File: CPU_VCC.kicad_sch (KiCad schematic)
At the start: 1 part

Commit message: Some DP and power work
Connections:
- net VCCSA: now reaches JCPU1.AA6 (VCCSA)
- net VCCSA: now also JCPU1.AA7 (VCCSA), JCPU1.AB6 (VCCSA), JCPU1.AB7 (VCCSA), JCPU1.AB8 (VCCSA), JCPU1.AC7 (VCCSA), JCPU1.AC8 (VCCSA), JCPU1.N7 (VCCSA), JCPU1.P7 (VCCSA), JCPU1.R7 (VCCSA), JCPU1.T7 (VCCSA), JCPU1.U7 (VCCSA), JCPU1.V7 (VCCSA), JCPU1.W7 (VCCSA), JCPU1.Y6 (VCCSA), JCPU1.Y7 (VCCSA), JCPU1.Y8 (VCCSA)
- net VCCIO: now reaches JCPU1.AJ23 (VCCIO)
- net VCCIO: now also JCPU1.AK11 (VCCIO), JCPU1.AK14 (VCCIO), JCPU1.AK24 (VCCIO), JCPU1.M8 (VCCIO), JCPU1.P8 (VCCIO), JCPU1.T8 (VCCIO), JCPU1.U8 (VCCIO), JCPU1.W8 (VCCIO)
- net VDDQ: now reaches JCPU1.AT18 (VDDQ)
- net VDDQ: now also JCPU1.AT21 (VDDQ), JCPU1.AU13 (VDDQ), JCPU1.AU15 (VDDQ), JCPU1.AU19 (VDDQ), JCPU1.AU23 (VDDQ), JCPU1.AV11 (VDDQ), JCPU1.AV17 (VDDQ), JCPU1.AV21 (VDDQ), JCPU1.AW10 (VDDQ), JCPU1.AW14 (VDDQ), JCPU1.AW25 (VDDQ), JCPU1.AY12 (VDDQ), JCPU1.AY16 (VDDQ), JCPU1.AY18 (VDDQ), JCPU1.AY23 (VDDQ)
- net VCCST: now reaches JCPU1.V5 (VCCST)
- net VCCST: now also JCPU1.V6 (VCCST)
- net VCC_CORE: now reaches JCPU1.A25 (VCC_CORE)
- net VCC_CORE: now also JCPU1.A26 (VCC_CORE), JCPU1.A27 (VCC_CORE), JCPU1.A28 (VCC_CORE), JCPU1.A29 (VCC_CORE), JCPU1.A30 (VCC_CORE), JCPU1.AJ11 (VCC_CORE), JCPU1.AJ12 (VCC_CORE), JCPU1.AJ13 (VCC_CORE), JCPU1.AJ14 (VCC_CORE), JCPU1.AJ15 (VCC_CORE), JCPU1.AJ16 (VCC_CORE), JCPU1.AJ17 (VCC_CORE), JCPU1.AJ18 (VCC_CORE), JCPU1.AJ19 (VCC_CORE), JCPU1.AJ20 (VCC_CORE), JCPU1.AJ21 (VCC_CORE), JCPU1.AJ25 (VCC_CORE), JCPU1.AJ26 (VCC_CORE), JCPU1.AJ27 (VCC_CORE), JCPU1.AJ28 (VCC_CORE), JCPU1.AJ29 (VCC_CORE), JCPU1.AK21 (VCC_CORE), JCPU1.B25 (VCC_CORE), JCPU1.B27 (VCC_CORE), JCPU1.B29 (VCC_CORE), JCPU1.B31 (VCC_CORE), JCPU1.B32 (VCC_CORE), JCPU1.B33 (VCC_CORE), JCPU1.B34 (VCC_CORE), JCPU1.B35 (VCC_CORE), JCPU1.B36 (VCC_CORE), JCPU1.B37 (VCC_CORE), JCPU1.C25 (VCC_CORE), JCPU1.C26 (VCC_CORE), JCPU1.C27 (VCC_CORE), JCPU1.C28 (VCC_CORE), JCPU1.C29 (VCC_CORE), JCPU1.C30 (VCC_CORE), JCPU1.C32 (VCC_CORE), JCPU1.C34 (VCC_CORE), JCPU1.C36 (VCC_CORE), JCPU1.D25 (VCC_CORE), JCPU1.D27 (VCC_CORE), JCPU1.D29 (VCC_CORE), JCPU1.D31 (VCC_CORE), JCPU1.D32 (VCC_CORE), JCPU1.D33 (VCC_CORE), JCPU1.D34 (VCC_CORE), JCPU1.D35 (VCC_CORE), JCPU1.D36 (VCC_CORE), JCPU1.E24 (VCC_CORE), JCPU1.E25 (VCC_CORE), JCPU1.E26 (VCC_CORE), JCPU1.E27 (VCC_CORE), JCPU1.E28 (VCC_CORE), JCPU1.E29 (VCC_CORE), JCPU1.E30 (VCC_CORE), JCPU1.E32 (VCC_CORE), JCPU1.E34 (VCC_CORE), JCPU1.E36 (VCC_CORE), JCPU1.F23 (VCC_CORE), JCPU1.F24 (VCC_CORE), JCPU1.F25 (VCC_CORE), JCPU1.F27 (VCC_CORE), JCPU1.F29 (VCC_CORE), JCPU1.F31 (VCC_CORE), JCPU1.F32 (VCC_CORE), JCPU1.F33 (VCC_CORE), JCPU1.F34 (VCC_CORE), JCPU1.F35 (VCC_CORE), JCPU1.F37 (VCC_CORE), JCPU1.G23 (VCC_CORE), JCPU1.G24 (VCC_CORE), JCPU1.G25 (VCC_CORE), JCPU1.G26 (VCC_CORE), JCPU1.G27 (VCC_CORE), JCPU1.G28 (VCC_CORE), JCPU1.G29 (VCC_CORE), JCPU1.G30 (VCC_CORE), JCPU1.G32 (VCC_CORE), JCPU1.G34 (VCC_CORE), JCPU1.G35 (VCC_CORE), JCPU1.H22 (VCC_CORE), JCPU1.H23 (VCC_CORE), JCPU1.H25 (VCC_CORE), JCPU1.H27 (VCC_CORE), JCPU1.H29 (VCC_CORE), JCPU1.H31 (VCC_CORE), JCPU1.H32 (VCC_CORE), JCPU1.H33 (VCC_CORE), JCPU1.H34 (VCC_CORE), JCPU1.J21 (VCC_CORE), JCPU1.J22 (VCC_CORE), JCPU1.J23 (VCC_CORE), JCPU1.J24 (VCC_CORE), JCPU1.J25 (VCC_CORE), JCPU1.J26 (VCC_CORE), JCPU1.J27 (VCC_CORE), JCPU1.J28 (VCC_CORE), JCPU1.J29 (VCC_CORE), JCPU1.J30 (VCC_CORE), JCPU1.J31 (VCC_CORE), JCPU1.J33 (VCC_CORE), JCPU1.J35 (VCC_CORE), JCPU1.K16 (VCC_CORE), JCPU1.K18 (VCC_CORE), JCPU1.K20 (VCC_CORE), JCPU1.K21 (VCC_CORE), JCPU1.K23 (VCC_CORE), JCPU1.K25 (VCC_CORE), JCPU1.K27 (VCC_CORE), JCPU1.K29 (VCC_CORE), JCPU1.K31 (VCC_CORE), JCPU1.K32 (VCC_CORE), JCPU1.K34 (VCC_CORE), JCPU1.L14 (VCC_CORE), JCPU1.L15 (VCC_CORE), JCPU1.L16 (VCC_CORE), JCPU1.L17 (VCC_CORE), JCPU1.L18 (VCC_CORE), JCPU1.L19 (VCC_CORE), JCPU1.L20 (VCC_CORE), JCPU1.L21 (VCC_CORE), JCPU1.L22 (VCC_CORE), JCPU1.L23 (VCC_CORE), JCPU1.L24 (VCC_CORE), JCPU1.L25 (VCC_CORE), JCPU1.L26 (VCC_CORE), JCPU1.L27 (VCC_CORE), JCPU1.L28 (VCC_CORE), JCPU1.L29 (VCC_CORE), JCPU1.L30 (VCC_CORE), JCPU1.L31 (VCC_CORE), JCPU1.L33 (VCC_CORE), JCPU1.M13 (VCC_CORE), JCPU1.M14 (VCC_CORE), JCPU1.M16 (VCC_CORE), JCPU1.M18 (VCC_CORE), JCPU1.M20 (VCC_CORE), JCPU1.M22 (VCC_CORE), JCPU1.M24 (VCC_CORE), JCPU1.M26 (VCC_CORE), JCPU1.M28 (VCC_CORE), JCPU1.M30 (VCC_CORE), JCPU1.M32 (VCC_CORE)
- net VCC_iGPU: now reaches JCPU1.AA34 (VCCGT)
- net VCC_iGPU: now also JCPU1.AA35 (VCCGT), JCPU1.AA36 (VCCGT), JCPU1.AA37 (VCCGT), JCPU1.AA38 (VCCGT), JCPU1.AB33 (VCCGT), JCPU1.AB34 (VCCGT), JCPU1.G36 (VCCGT), JCPU1.G37 (VCCGT), JCPU1.G38 (VCCGT), JCPU1.G39 (VCCGT), JCPU1.G40 (VCCGT), JCPU1.H36 (VCCGT), JCPU1.H38 (VCCGT), JCPU1.H40 (VCCGT), JCPU1.J36 (VCCGT), JCPU1.J37 (VCCGT), JCPU1.J38 (VCCGT), JCPU1.J39 (VCCGT), JCPU1.J40 (VCCGT), JCPU1.K36 (VCCGT), JCPU1.K38 (VCCGT), JCPU1.K40 (VCCGT), JCPU1.L34 (VCCGT), JCPU1.L35 (VCCGT), JCPU1.L36 (VCCGT), JCPU1.L37 (VCCGT), JCPU1.L38 (VCCGT), JCPU1.L39 (VCCGT), JCPU1.L40 (VCCGT), JCPU1.M33 (VCCGT), JCPU1.M34 (VCCGT), JCPU1.M36 (VCCGT), JCPU1.M38 (VCCGT), JCPU1.M40 (VCCGT), JCPU1.N34 (VCCGT), JCPU1.N35 (VCCGT), JCPU1.N36 (VCCGT), JCPU1.N37 (VCCGT), JCPU1.N38 (VCCGT), JCPU1.N39 (VCCGT), JCPU1.N40 (VCCGT), JCPU1.P33 (VCCGT), JCPU1.P34 (VCCGT), JCPU1.P36 (VCCGT), JCPU1.P38 (VCCGT), JCPU1.P40 (VCCGT), JCPU1.R34 (VCCGT), JCPU1.R35 (VCCGT), JCPU1.R36 (VCCGT), JCPU1.R37 (VCCGT), JCPU1.R38 (VCCGT), JCPU1.R39 (VCCGT), JCPU1.R40 (VCCGT), JCPU1.T33 (VCCGT), JCPU1.T34 (VCCGT), JCPU1.T36 (VCCGT), JCPU1.T38 (VCCGT), JCPU1.T40 (VCCGT), JCPU1.U34 (VCCGT), JCPU1.U35 (VCCGT), JCPU1.U36 (VCCGT), JCPU1.U37 (VCCGT), JCPU1.U38 (VCCGT), JCPU1.U39 (VCCGT), JCPU1.U40 (VCCGT), JCPU1.V33 (VCCGT), JCPU1.V34 (VCCGT), JCPU1.V36 (VCCGT), JCPU1.V38 (VCCGT), JCPU1.V40 (VCCGT), JCPU1.W34 (VCCGT), JCPU1.W35 (VCCGT), JCPU1.W36 (VCCGT), JCPU1.W37 (VCCGT), JCPU1.W38 (VCCGT), JCPU1.Y33 (VCCGT), JCPU1.Y34 (VCCGT), JCPU1.Y36 (VCCGT), JCPU1.Y38 (VCCGT)

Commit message: Added LGA1151 socket bracket holes
stolen from another lga1151 footprint that has wrong pin numbers....
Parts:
- JCPU1: footprint A-my-stuff:LGA-1151_L47.1-W42.5-P0.91_PE115127-4041-01H -> A-my-stuff:LGA1151_TE-2287402-1
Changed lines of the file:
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@@
 			)
 		)
-		(property "Footprint" "A-my-stuff:LGA-1151_L47.1-W42.5-P0.91_PE115127-4041-01H"
+		(property "Footprint" "A-my-stuff:LGA1151_TE-2287402-1"
 			(at 203.2 256.54 0)
 			(effects
@@
 			)
 		)
-		(property "Footprint" "A-my-stuff:LGA-1151_L47.1-W42.5-P0.91_PE115127-4041-01H"
+		(property "Footprint" "A-my-stuff:LGA1151_TE-2287402-1"
 			(at 76.2 256.54 0)
 			(effects
@@
 			)
 		)
-		(property "Footprint" "A-my-stuff:LGA-1151_L47.1-W42.5-P0.91_PE115127-4041-01H"
+		(property "Footprint" "A-my-stuff:LGA1151_TE-2287402-1"
 			(at 139.7 256.54 0)
 			(effects

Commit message: Added CPU CFG resistors
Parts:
- JCPU1: footprint A-my-stuff:LGA1151_TE-2287402-1 -> A-my-stuff:LGA-1151_L47.1-W42.5-P0.91_PE115127-4041-01H
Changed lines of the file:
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@@
 			)
 		)
-		(property "Footprint" "A-my-stuff:LGA1151_TE-2287402-1"
+		(property "Footprint" "A-my-stuff:LGA-1151_L47.1-W42.5-P0.91_PE115127-4041-01H"
 			(at 203.2 256.54 0)
 			(effects
@@
 			)
 		)
-		(property "Footprint" "A-my-stuff:LGA1151_TE-2287402-1"
+		(property "Footprint" "A-my-stuff:LGA-1151_L47.1-W42.5-P0.91_PE115127-4041-01H"
 			(at 76.2 256.54 0)
 			(effects
@@
 			)
 		)
-		(property "Footprint" "A-my-stuff:LGA1151_TE-2287402-1"
+		(property "Footprint" "A-my-stuff:LGA-1151_L47.1-W42.5-P0.91_PE115127-4041-01H"
 			(at 139.7 256.54 0)
 			(effects

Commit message: stroopwafel.exe
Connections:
- net VCCIO: no longer JCPU1.AJ23 (VCCIO), JCPU1.AK11 (VCCIO), JCPU1.AK14 (VCCIO), JCPU1.AK24 (VCCIO), JCPU1.M8 (VCCIO), JCPU1.P8 (VCCIO), JCPU1.T8 (VCCIO), JCPU1.U8 (VCCIO), JCPU1.W8 (VCCIO)
- net VCCSA: no longer JCPU1.AA6 (VCCSA), JCPU1.AA7 (VCCSA), JCPU1.AB6 (VCCSA), JCPU1.AB7 (VCCSA), JCPU1.AB8 (VCCSA), JCPU1.AC7 (VCCSA), JCPU1.AC8 (VCCSA), JCPU1.N7 (VCCSA), JCPU1.P7 (VCCSA), JCPU1.R7 (VCCSA), JCPU1.T7 (VCCSA), JCPU1.U7 (VCCSA), JCPU1.V7 (VCCSA), JCPU1.W7 (VCCSA), JCPU1.Y6 (VCCSA), JCPU1.Y7 (VCCSA), JCPU1.Y8 (VCCSA)
- net VCCST: no longer JCPU1.V5 (VCCST), JCPU1.V6 (VCCST)
- net VCC_CORE: no longer JCPU1.A25 (VCC_CORE), JCPU1.A26 (VCC_CORE), JCPU1.A27 (VCC_CORE), JCPU1.A28 (VCC_CORE), JCPU1.A29 (VCC_CORE), JCPU1.A30 (VCC_CORE), JCPU1.AJ11 (VCC_CORE), JCPU1.AJ12 (VCC_CORE), JCPU1.AJ13 (VCC_CORE), JCPU1.AJ14 (VCC_CORE), JCPU1.AJ15 (VCC_CORE), JCPU1.AJ16 (VCC_CORE), JCPU1.AJ17 (VCC_CORE), JCPU1.AJ18 (VCC_CORE), JCPU1.AJ19 (VCC_CORE), JCPU1.AJ20 (VCC_CORE), JCPU1.AJ21 (VCC_CORE), JCPU1.AJ25 (VCC_CORE), JCPU1.AJ26 (VCC_CORE), JCPU1.AJ27 (VCC_CORE), JCPU1.AJ28 (VCC_CORE), JCPU1.AJ29 (VCC_CORE), JCPU1.AK21 (VCC_CORE), JCPU1.B25 (VCC_CORE), JCPU1.B27 (VCC_CORE), JCPU1.B29 (VCC_CORE), JCPU1.B31 (VCC_CORE), JCPU1.B32 (VCC_CORE), JCPU1.B33 (VCC_CORE), JCPU1.B34 (VCC_CORE), JCPU1.B35 (VCC_CORE), JCPU1.B36 (VCC_CORE), JCPU1.B37 (VCC_CORE), JCPU1.C25 (VCC_CORE), JCPU1.C26 (VCC_CORE), JCPU1.C27 (VCC_CORE), JCPU1.C28 (VCC_CORE), JCPU1.C29 (VCC_CORE), JCPU1.C30 (VCC_CORE), JCPU1.C32 (VCC_CORE), JCPU1.C34 (VCC_CORE), JCPU1.C36 (VCC_CORE), JCPU1.D25 (VCC_CORE), JCPU1.D27 (VCC_CORE), JCPU1.D29 (VCC_CORE), JCPU1.D31 (VCC_CORE), JCPU1.D32 (VCC_CORE), JCPU1.D33 (VCC_CORE), JCPU1.D34 (VCC_CORE), JCPU1.D35 (VCC_CORE), JCPU1.D36 (VCC_CORE), JCPU1.E24 (VCC_CORE), JCPU1.E25 (VCC_CORE), JCPU1.E26 (VCC_CORE), JCPU1.E27 (VCC_CORE), JCPU1.E28 (VCC_CORE), JCPU1.E29 (VCC_CORE), JCPU1.E30 (VCC_CORE), JCPU1.E32 (VCC_CORE), JCPU1.E34 (VCC_CORE), JCPU1.E36 (VCC_CORE), JCPU1.F23 (VCC_CORE), JCPU1.F24 (VCC_CORE), JCPU1.F25 (VCC_CORE), JCPU1.F27 (VCC_CORE), JCPU1.F29 (VCC_CORE), JCPU1.F31 (VCC_CORE), JCPU1.F32 (VCC_CORE), JCPU1.F33 (VCC_CORE), JCPU1.F34 (VCC_CORE), JCPU1.F35 (VCC_CORE), JCPU1.F37 (VCC_CORE), JCPU1.G23 (VCC_CORE), JCPU1.G24 (VCC_CORE), JCPU1.G25 (VCC_CORE), JCPU1.G26 (VCC_CORE), JCPU1.G27 (VCC_CORE), JCPU1.G28 (VCC_CORE), JCPU1.G29 (VCC_CORE), JCPU1.G30 (VCC_CORE), JCPU1.G32 (VCC_CORE), JCPU1.G34 (VCC_CORE), JCPU1.G35 (VCC_CORE), JCPU1.H22 (VCC_CORE), JCPU1.H23 (VCC_CORE), JCPU1.H25 (VCC_CORE), JCPU1.H27 (VCC_CORE), JCPU1.H29 (VCC_CORE), JCPU1.H31 (VCC_CORE), JCPU1.H32 (VCC_CORE), JCPU1.H33 (VCC_CORE), JCPU1.H34 (VCC_CORE), JCPU1.J21 (VCC_CORE), JCPU1.J22 (VCC_CORE), JCPU1.J23 (VCC_CORE), JCPU1.J24 (VCC_CORE), JCPU1.J25 (VCC_CORE), JCPU1.J26 (VCC_CORE), JCPU1.J27 (VCC_CORE), JCPU1.J28 (VCC_CORE), JCPU1.J29 (VCC_CORE), JCPU1.J30 (VCC_CORE), JCPU1.J31 (VCC_CORE), JCPU1.J33 (VCC_CORE), JCPU1.J35 (VCC_CORE), JCPU1.K16 (VCC_CORE), JCPU1.K18 (VCC_CORE), JCPU1.K20 (VCC_CORE), JCPU1.K21 (VCC_CORE), JCPU1.K23 (VCC_CORE), JCPU1.K25 (VCC_CORE), JCPU1.K27 (VCC_CORE), JCPU1.K29 (VCC_CORE), JCPU1.K31 (VCC_CORE), JCPU1.K32 (VCC_CORE), JCPU1.K34 (VCC_CORE), JCPU1.L14 (VCC_CORE), JCPU1.L15 (VCC_CORE), JCPU1.L16 (VCC_CORE), JCPU1.L17 (VCC_CORE), JCPU1.L18 (VCC_CORE), JCPU1.L19 (VCC_CORE), JCPU1.L20 (VCC_CORE), JCPU1.L21 (VCC_CORE), JCPU1.L22 (VCC_CORE), JCPU1.L23 (VCC_CORE), JCPU1.L24 (VCC_CORE), JCPU1.L25 (VCC_CORE), JCPU1.L26 (VCC_CORE), JCPU1.L27 (VCC_CORE), JCPU1.L28 (VCC_CORE), JCPU1.L29 (VCC_CORE), JCPU1.L30 (VCC_CORE), JCPU1.L31 (VCC_CORE), JCPU1.L33 (VCC_CORE), JCPU1.M13 (VCC_CORE), JCPU1.M14 (VCC_CORE), JCPU1.M16 (VCC_CORE), JCPU1.M18 (VCC_CORE), JCPU1.M20 (VCC_CORE), JCPU1.M22 (VCC_CORE), JCPU1.M24 (VCC_CORE), JCPU1.M26 (VCC_CORE), JCPU1.M28 (VCC_CORE), JCPU1.M30 (VCC_CORE), JCPU1.M32 (VCC_CORE)
- net VCC_iGPU: no longer JCPU1.AA34 (VCCGT), JCPU1.AA35 (VCCGT), JCPU1.AA36 (VCCGT), JCPU1.AA37 (VCCGT), JCPU1.AA38 (VCCGT), JCPU1.AB33 (VCCGT), JCPU1.AB34 (VCCGT), JCPU1.G36 (VCCGT), JCPU1.G37 (VCCGT), JCPU1.G38 (VCCGT), JCPU1.G39 (VCCGT), JCPU1.G40 (VCCGT), JCPU1.H36 (VCCGT), JCPU1.H38 (VCCGT), JCPU1.H40 (VCCGT), JCPU1.J36 (VCCGT), JCPU1.J37 (VCCGT), JCPU1.J38 (VCCGT), JCPU1.J39 (VCCGT), JCPU1.J40 (VCCGT), JCPU1.K36 (VCCGT), JCPU1.K38 (VCCGT), JCPU1.K40 (VCCGT), JCPU1.L34 (VCCGT), JCPU1.L35 (VCCGT), JCPU1.L36 (VCCGT), JCPU1.L37 (VCCGT), JCPU1.L38 (VCCGT), JCPU1.L39 (VCCGT), JCPU1.L40 (VCCGT), JCPU1.M33 (VCCGT), JCPU1.M34 (VCCGT), JCPU1.M36 (VCCGT), JCPU1.M38 (VCCGT), JCPU1.M40 (VCCGT), JCPU1.N34 (VCCGT), JCPU1.N35 (VCCGT), JCPU1.N36 (VCCGT), JCPU1.N37 (VCCGT), JCPU1.N38 (VCCGT), JCPU1.N39 (VCCGT), JCPU1.N40 (VCCGT), JCPU1.P33 (VCCGT), JCPU1.P34 (VCCGT), JCPU1.P36 (VCCGT), JCPU1.P38 (VCCGT), JCPU1.P40 (VCCGT), JCPU1.R34 (VCCGT), JCPU1.R35 (VCCGT), JCPU1.R36 (VCCGT), JCPU1.R37 (VCCGT), JCPU1.R38 (VCCGT), JCPU1.R39 (VCCGT), JCPU1.R40 (VCCGT), JCPU1.T33 (VCCGT), JCPU1.T34 (VCCGT), JCPU1.T36 (VCCGT), JCPU1.T38 (VCCGT), JCPU1.T40 (VCCGT), JCPU1.U34 (VCCGT), JCPU1.U35 (VCCGT), JCPU1.U36 (VCCGT), JCPU1.U37 (VCCGT), JCPU1.U38 (VCCGT), JCPU1.U39 (VCCGT), JCPU1.U40 (VCCGT), JCPU1.V33 (VCCGT), JCPU1.V34 (VCCGT), JCPU1.V36 (VCCGT), JCPU1.V38 (VCCGT), JCPU1.V40 (VCCGT), JCPU1.W34 (VCCGT), JCPU1.W35 (VCCGT), JCPU1.W36 (VCCGT), JCPU1.W37 (VCCGT), JCPU1.W38 (VCCGT), JCPU1.Y33 (VCCGT), JCPU1.Y34 (VCCGT), JCPU1.Y36 (VCCGT), JCPU1.Y38 (VCCGT)
- net VDDQ: no longer JCPU1.AT18 (VDDQ), JCPU1.AT21 (VDDQ), JCPU1.AU13 (VDDQ), JCPU1.AU15 (VDDQ), JCPU1.AU19 (VDDQ), JCPU1.AU23 (VDDQ), JCPU1.AV11 (VDDQ), JCPU1.AV17 (VDDQ), JCPU1.AV21 (VDDQ), JCPU1.AW10 (VDDQ), JCPU1.AW14 (VDDQ), JCPU1.AW25 (VDDQ), JCPU1.AY12 (VDDQ), JCPU1.AY16 (VDDQ), JCPU1.AY18 (VDDQ), JCPU1.AY23 (VDDQ)
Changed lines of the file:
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@@
 		(lib_id "A-my-stuff:Intel_CFL_1151")
 		(at 203.2 144.78 0)
-		(unit 9)
+		(unit 1)
 		(exclude_from_sim no)
 		(in_bom yes)
@@
 		(pin "J5"
 		)
-		(instances
-			(project ""
-				(path "/4bc771b8-eb19-46d0-8798-27231a7c6e83/061fe2d6-87c2-48c2-90bb-0928700512fc"
-					(reference "JCPU1")
-					(unit 9)
-				)
-				(path "/4bc771b8-eb19-46d0-8798-27231a7c6e83/5036d382-d60b-4069-a42a-4bbea2c68172"
-					(reference "JCPU1")
-					(unit 9)
-				)
-			)
-		)
 	)
 	(symbol
@@
 		(lib_id "A-my-stuff:Intel_CFL_1151")
 		(at 76.2 144.78 0)
-		(unit 7)
+		(unit 1)
 		(exclude_from_sim no)
 		(in_bom yes)
@@
 		(pin "J5"
 		)
-		(instances
-			(project ""
-				(path "/4bc771b8-eb19-46d0-8798-27231a7c6e83/061fe2d6-87c2-48c2-90bb-0928700512fc"
-					(reference "JCPU1")
-					(unit 7)
-				)
-				(path "/4bc771b8-eb19-46d0-8798-27231a7c6e83/5036d382-d60b-4069-a42a-4bbea2c68172"
-					(reference "JCPU1")
-					(unit 7)
-				)
-			)
-		)
 	)
 	(symbol
@@
 		(lib_id "A-my-stuff:Intel_CFL_1151")
 		(at 139.7 144.78 0)
-		(unit 8)
+		(unit 1)
 		(exclude_from_sim no)
 		(in_bom yes)
@@
 		(pin "J5"
 		)
-		(instances
-			(project ""
-				(path "/4bc771b8-eb19-46d0-8798-27231a7c6e83/061fe2d6-87c2-48c2-90bb-0928700512fc"
-					(reference "JCPU1")
-					(unit 8)
-				)
-				(path "/4bc771b8-eb19-46d0-8798-27231a7c6e83/5036d382-d60b-4069-a42a-4bbea2c68172"
-					(reference "JCPU1")
-					(unit 8)
-				)
-			)
-		)
 	)
 	(symbol
@@
 		(pin "1"
 		)
-		(instances
-			(project ""
-				(path "/4bc771b8-eb19-46d0-8798-27231a7c6e83/5036d382-d60b-4069-a42a-4bbea2c68172"
-					(reference "#PWR011")
-					(unit 1)
-				)
-			)
-		)
 	)

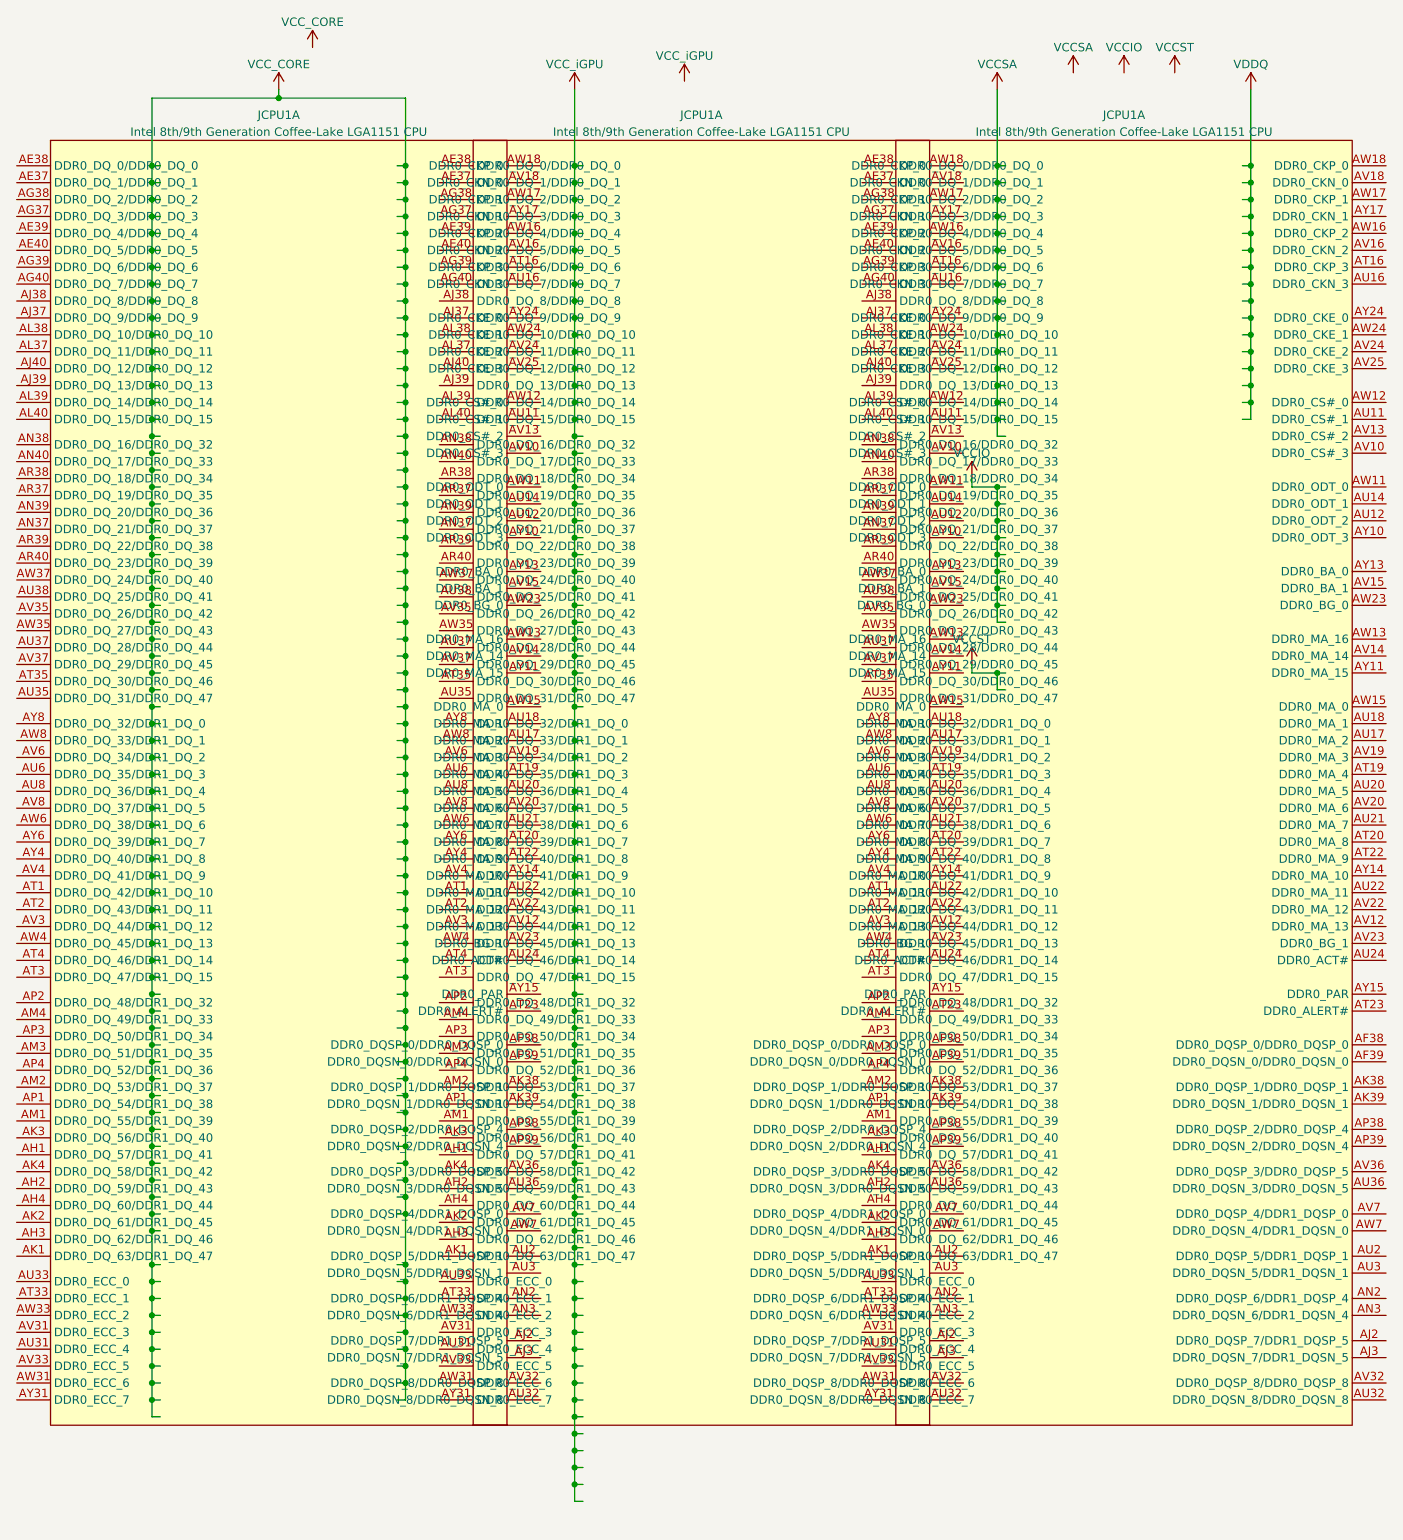
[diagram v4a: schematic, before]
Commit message: Fixed entire schematic being broken
somehow every symbol with index 1 broke and updating the pcb stopped working. how does that even happen. oh well it's fixed now
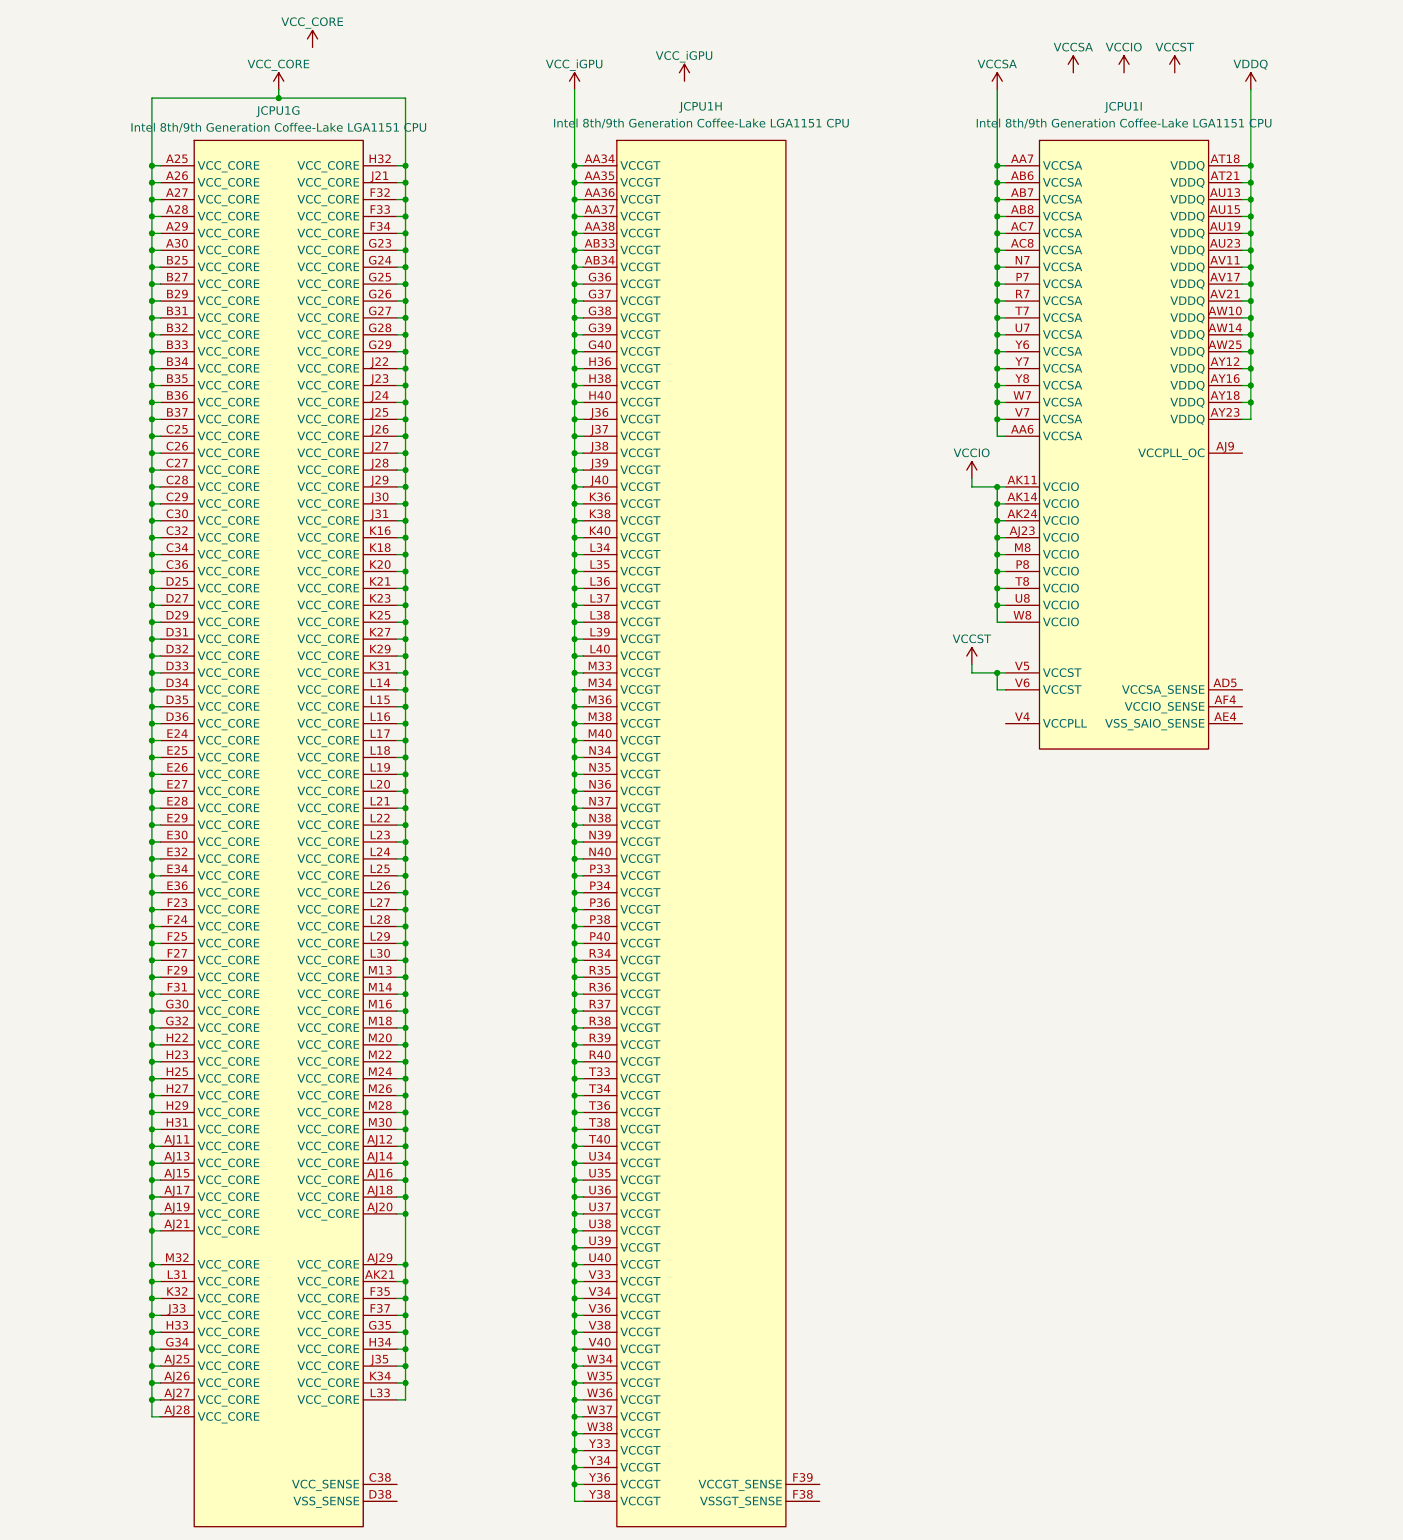
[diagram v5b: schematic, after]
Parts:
- removed JCPU1 (x3): Intel 8th/9th Generation Coffee-Lake LGA1151 CPU, A-my-stuff:LGA-1151_L47.1-W42.5-P0.91_PE115127-4041-01H, symbol A-my-stuff:Intel_CFL_1151
- added JCPU1: Intel 8th/9th Generation Coffee-Lake LGA1151 CPU, A-my-stuff:LGA-1151_L47.1-W42.5-P0.91_PE115127-4041-01H, symbol A-my-stuff:Intel_CFL_1151
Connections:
- net VCCIO: now also JCPU1.AJ23 (VCCIO), JCPU1.AK11 (VCCIO), JCPU1.AK14 (VCCIO), JCPU1.AK24 (VCCIO), JCPU1.M8 (VCCIO), JCPU1.P8 (VCCIO), JCPU1.T8 (VCCIO), JCPU1.U8 (VCCIO), JCPU1.W8 (VCCIO)
- net VCCSA: now also JCPU1.AA6 (VCCSA), JCPU1.AA7 (VCCSA), JCPU1.AB6 (VCCSA), JCPU1.AB7 (VCCSA), JCPU1.AB8 (VCCSA), JCPU1.AC7 (VCCSA), JCPU1.AC8 (VCCSA), JCPU1.N7 (VCCSA), JCPU1.P7 (VCCSA), JCPU1.R7 (VCCSA), JCPU1.T7 (VCCSA), JCPU1.U7 (VCCSA), JCPU1.V7 (VCCSA), JCPU1.W7 (VCCSA), JCPU1.Y6 (VCCSA), JCPU1.Y7 (VCCSA), JCPU1.Y8 (VCCSA)
- net VCCST: now also JCPU1.V5 (VCCST), JCPU1.V6 (VCCST)
- net VCC_CORE: now also JCPU1.A25 (VCC_CORE), JCPU1.A26 (VCC_CORE), JCPU1.A27 (VCC_CORE), JCPU1.A28 (VCC_CORE), JCPU1.A29 (VCC_CORE), JCPU1.A30 (VCC_CORE), JCPU1.AJ11 (VCC_CORE), JCPU1.AJ12 (VCC_CORE), JCPU1.AJ13 (VCC_CORE), JCPU1.AJ14 (VCC_CORE), JCPU1.AJ15 (VCC_CORE), JCPU1.AJ16 (VCC_CORE), JCPU1.AJ17 (VCC_CORE), JCPU1.AJ18 (VCC_CORE), JCPU1.AJ19 (VCC_CORE), JCPU1.AJ20 (VCC_CORE), JCPU1.AJ21 (VCC_CORE), JCPU1.AJ25 (VCC_CORE), JCPU1.AJ26 (VCC_CORE), JCPU1.AJ27 (VCC_CORE), JCPU1.AJ28 (VCC_CORE), JCPU1.AJ29 (VCC_CORE), JCPU1.AK21 (VCC_CORE), JCPU1.B25 (VCC_CORE), JCPU1.B27 (VCC_CORE), JCPU1.B29 (VCC_CORE), JCPU1.B31 (VCC_CORE), JCPU1.B32 (VCC_CORE), JCPU1.B33 (VCC_CORE), JCPU1.B34 (VCC_CORE), JCPU1.B35 (VCC_CORE), JCPU1.B36 (VCC_CORE), JCPU1.B37 (VCC_CORE), JCPU1.C25 (VCC_CORE), JCPU1.C26 (VCC_CORE), JCPU1.C27 (VCC_CORE), JCPU1.C28 (VCC_CORE), JCPU1.C29 (VCC_CORE), JCPU1.C30 (VCC_CORE), JCPU1.C32 (VCC_CORE), JCPU1.C34 (VCC_CORE), JCPU1.C36 (VCC_CORE), JCPU1.D25 (VCC_CORE), JCPU1.D27 (VCC_CORE), JCPU1.D29 (VCC_CORE), JCPU1.D31 (VCC_CORE), JCPU1.D32 (VCC_CORE), JCPU1.D33 (VCC_CORE), JCPU1.D34 (VCC_CORE), JCPU1.D35 (VCC_CORE), JCPU1.D36 (VCC_CORE), JCPU1.E24 (VCC_CORE), JCPU1.E25 (VCC_CORE), JCPU1.E26 (VCC_CORE), JCPU1.E27 (VCC_CORE), JCPU1.E28 (VCC_CORE), JCPU1.E29 (VCC_CORE), JCPU1.E30 (VCC_CORE), JCPU1.E32 (VCC_CORE), JCPU1.E34 (VCC_CORE), JCPU1.E36 (VCC_CORE), JCPU1.F23 (VCC_CORE), JCPU1.F24 (VCC_CORE), JCPU1.F25 (VCC_CORE), JCPU1.F27 (VCC_CORE), JCPU1.F29 (VCC_CORE), JCPU1.F31 (VCC_CORE), JCPU1.F32 (VCC_CORE), JCPU1.F33 (VCC_CORE), JCPU1.F34 (VCC_CORE), JCPU1.F35 (VCC_CORE), JCPU1.F37 (VCC_CORE), JCPU1.G23 (VCC_CORE), JCPU1.G24 (VCC_CORE), JCPU1.G25 (VCC_CORE), JCPU1.G26 (VCC_CORE), JCPU1.G27 (VCC_CORE), JCPU1.G28 (VCC_CORE), JCPU1.G29 (VCC_CORE), JCPU1.G30 (VCC_CORE), JCPU1.G32 (VCC_CORE), JCPU1.G34 (VCC_CORE), JCPU1.G35 (VCC_CORE), JCPU1.H22 (VCC_CORE), JCPU1.H23 (VCC_CORE), JCPU1.H25 (VCC_CORE), JCPU1.H27 (VCC_CORE), JCPU1.H29 (VCC_CORE), JCPU1.H31 (VCC_CORE), JCPU1.H32 (VCC_CORE), JCPU1.H33 (VCC_CORE), JCPU1.H34 (VCC_CORE), JCPU1.J21 (VCC_CORE), JCPU1.J22 (VCC_CORE), JCPU1.J23 (VCC_CORE), JCPU1.J24 (VCC_CORE), JCPU1.J25 (VCC_CORE), JCPU1.J26 (VCC_CORE), JCPU1.J27 (VCC_CORE), JCPU1.J28 (VCC_CORE), JCPU1.J29 (VCC_CORE), JCPU1.J30 (VCC_CORE), JCPU1.J31 (VCC_CORE), JCPU1.J33 (VCC_CORE), JCPU1.J35 (VCC_CORE), JCPU1.K16 (VCC_CORE), JCPU1.K18 (VCC_CORE), JCPU1.K20 (VCC_CORE), JCPU1.K21 (VCC_CORE), JCPU1.K23 (VCC_CORE), JCPU1.K25 (VCC_CORE), JCPU1.K27 (VCC_CORE), JCPU1.K29 (VCC_CORE), JCPU1.K31 (VCC_CORE), JCPU1.K32 (VCC_CORE), JCPU1.K34 (VCC_CORE), JCPU1.L14 (VCC_CORE), JCPU1.L15 (VCC_CORE), JCPU1.L16 (VCC_CORE), JCPU1.L17 (VCC_CORE), JCPU1.L18 (VCC_CORE), JCPU1.L19 (VCC_CORE), JCPU1.L20 (VCC_CORE), JCPU1.L21 (VCC_CORE), JCPU1.L22 (VCC_CORE), JCPU1.L23 (VCC_CORE), JCPU1.L24 (VCC_CORE), JCPU1.L25 (VCC_CORE), JCPU1.L26 (VCC_CORE), JCPU1.L27 (VCC_CORE), JCPU1.L28 (VCC_CORE), JCPU1.L29 (VCC_CORE), JCPU1.L30 (VCC_CORE), JCPU1.L31 (VCC_CORE), JCPU1.L33 (VCC_CORE), JCPU1.M13 (VCC_CORE), JCPU1.M14 (VCC_CORE), JCPU1.M16 (VCC_CORE), JCPU1.M18 (VCC_CORE), JCPU1.M20 (VCC_CORE), JCPU1.M22 (VCC_CORE), JCPU1.M24 (VCC_CORE), JCPU1.M26 (VCC_CORE), JCPU1.M28 (VCC_CORE), JCPU1.M30 (VCC_CORE), JCPU1.M32 (VCC_CORE)
- net VCC_iGPU: now also JCPU1.AA34 (VCCGT), JCPU1.AA35 (VCCGT), JCPU1.AA36 (VCCGT), JCPU1.AA37 (VCCGT), JCPU1.AA38 (VCCGT), JCPU1.AB33 (VCCGT), JCPU1.AB34 (VCCGT), JCPU1.G36 (VCCGT), JCPU1.G37 (VCCGT), JCPU1.G38 (VCCGT), JCPU1.G39 (VCCGT), JCPU1.G40 (VCCGT), JCPU1.H36 (VCCGT), JCPU1.H38 (VCCGT), JCPU1.H40 (VCCGT), JCPU1.J36 (VCCGT), JCPU1.J37 (VCCGT), JCPU1.J38 (VCCGT), JCPU1.J39 (VCCGT), JCPU1.J40 (VCCGT), JCPU1.K36 (VCCGT), JCPU1.K38 (VCCGT), JCPU1.K40 (VCCGT), JCPU1.L34 (VCCGT), JCPU1.L35 (VCCGT), JCPU1.L36 (VCCGT), JCPU1.L37 (VCCGT), JCPU1.L38 (VCCGT), JCPU1.L39 (VCCGT), JCPU1.L40 (VCCGT), JCPU1.M33 (VCCGT), JCPU1.M34 (VCCGT), JCPU1.M36 (VCCGT), JCPU1.M38 (VCCGT), JCPU1.M40 (VCCGT), JCPU1.N34 (VCCGT), JCPU1.N35 (VCCGT), JCPU1.N36 (VCCGT), JCPU1.N37 (VCCGT), JCPU1.N38 (VCCGT), JCPU1.N39 (VCCGT), JCPU1.N40 (VCCGT), JCPU1.P33 (VCCGT), JCPU1.P34 (VCCGT), JCPU1.P36 (VCCGT), JCPU1.P38 (VCCGT), JCPU1.P40 (VCCGT), JCPU1.R34 (VCCGT), JCPU1.R35 (VCCGT), JCPU1.R36 (VCCGT), JCPU1.R37 (VCCGT), JCPU1.R38 (VCCGT), JCPU1.R39 (VCCGT), JCPU1.R40 (VCCGT), JCPU1.T33 (VCCGT), JCPU1.T34 (VCCGT), JCPU1.T36 (VCCGT), JCPU1.T38 (VCCGT), JCPU1.T40 (VCCGT), JCPU1.U34 (VCCGT), JCPU1.U35 (VCCGT), JCPU1.U36 (VCCGT), JCPU1.U37 (VCCGT), JCPU1.U38 (VCCGT), JCPU1.U39 (VCCGT), JCPU1.U40 (VCCGT), JCPU1.V33 (VCCGT), JCPU1.V34 (VCCGT), JCPU1.V36 (VCCGT), JCPU1.V38 (VCCGT), JCPU1.V40 (VCCGT), JCPU1.W34 (VCCGT), JCPU1.W35 (VCCGT), JCPU1.W36 (VCCGT), JCPU1.W37 (VCCGT), JCPU1.W38 (VCCGT), JCPU1.Y33 (VCCGT), JCPU1.Y34 (VCCGT), JCPU1.Y36 (VCCGT), JCPU1.Y38 (VCCGT)
- net VDDQ: now also JCPU1.AT18 (VDDQ), JCPU1.AT21 (VDDQ), JCPU1.AU13 (VDDQ), JCPU1.AU15 (VDDQ), JCPU1.AU19 (VDDQ), JCPU1.AU23 (VDDQ), JCPU1.AV11 (VDDQ), JCPU1.AV17 (VDDQ), JCPU1.AV21 (VDDQ), JCPU1.AW10 (VDDQ), JCPU1.AW14 (VDDQ), JCPU1.AW25 (VDDQ), JCPU1.AY12 (VDDQ), JCPU1.AY16 (VDDQ), JCPU1.AY18 (VDDQ), JCPU1.AY23 (VDDQ)

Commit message: nooo they be stealin my stroopwafel
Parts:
- added unit 8 of JCPU1
- added unit 9 of JCPU1
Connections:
- net VCCIO: now also JCPU1.AJ23 (VCCIO), JCPU1.AK11 (VCCIO), JCPU1.AK14 (VCCIO), JCPU1.AK24 (VCCIO), JCPU1.M8 (VCCIO), JCPU1.P8 (VCCIO), JCPU1.T8 (VCCIO), JCPU1.U8 (VCCIO), JCPU1.W8 (VCCIO); no longer JCPU1.AJ23 (VCCIO), JCPU1.AK11 (VCCIO), JCPU1.AK14 (VCCIO), JCPU1.AK24 (VCCIO), JCPU1.M8 (VCCIO), JCPU1.P8 (VCCIO), JCPU1.T8 (VCCIO), JCPU1.U8 (VCCIO), JCPU1.W8 (VCCIO)
- net VCCSA: now also JCPU1.AA6 (VCCSA), JCPU1.AA7 (VCCSA), JCPU1.AB6 (VCCSA), JCPU1.AB7 (VCCSA), JCPU1.AB8 (VCCSA), JCPU1.AC7 (VCCSA), JCPU1.AC8 (VCCSA), JCPU1.N7 (VCCSA), JCPU1.P7 (VCCSA), JCPU1.R7 (VCCSA), JCPU1.T7 (VCCSA), JCPU1.U7 (VCCSA), JCPU1.V7 (VCCSA), JCPU1.W7 (VCCSA), JCPU1.Y6 (VCCSA), JCPU1.Y7 (VCCSA), JCPU1.Y8 (VCCSA); no longer JCPU1.AA6 (VCCSA), JCPU1.AA7 (VCCSA), JCPU1.AB6 (VCCSA), JCPU1.AB7 (VCCSA), JCPU1.AB8 (VCCSA), JCPU1.AC7 (VCCSA), JCPU1.AC8 (VCCSA), JCPU1.N7 (VCCSA), JCPU1.P7 (VCCSA), JCPU1.R7 (VCCSA), JCPU1.T7 (VCCSA), JCPU1.U7 (VCCSA), JCPU1.V7 (VCCSA), JCPU1.W7 (VCCSA), JCPU1.Y6 (VCCSA), JCPU1.Y7 (VCCSA), JCPU1.Y8 (VCCSA)
- net VCCST: now also JCPU1.V5 (VCCST), JCPU1.V6 (VCCST); no longer JCPU1.V5 (VCCST), JCPU1.V6 (VCCST)
- net VCC_iGPU: now also JCPU1.AA34 (VCCGT), JCPU1.AA35 (VCCGT), JCPU1.AA36 (VCCGT), JCPU1.AA37 (VCCGT), JCPU1.AA38 (VCCGT), JCPU1.AB33 (VCCGT), JCPU1.AB34 (VCCGT), JCPU1.G36 (VCCGT), JCPU1.G37 (VCCGT), JCPU1.G38 (VCCGT), JCPU1.G39 (VCCGT), JCPU1.G40 (VCCGT), JCPU1.H36 (VCCGT), JCPU1.H38 (VCCGT), JCPU1.H40 (VCCGT), JCPU1.J36 (VCCGT), JCPU1.J37 (VCCGT), JCPU1.J38 (VCCGT), JCPU1.J39 (VCCGT), JCPU1.J40 (VCCGT), JCPU1.K36 (VCCGT), JCPU1.K38 (VCCGT), JCPU1.K40 (VCCGT), JCPU1.L34 (VCCGT), JCPU1.L35 (VCCGT), JCPU1.L36 (VCCGT), JCPU1.L37 (VCCGT), JCPU1.L38 (VCCGT), JCPU1.L39 (VCCGT), JCPU1.L40 (VCCGT), JCPU1.M33 (VCCGT), JCPU1.M34 (VCCGT), JCPU1.M36 (VCCGT), JCPU1.M38 (VCCGT), JCPU1.M40 (VCCGT), JCPU1.N34 (VCCGT), JCPU1.N35 (VCCGT), JCPU1.N36 (VCCGT), JCPU1.N37 (VCCGT), JCPU1.N38 (VCCGT), JCPU1.N39 (VCCGT), JCPU1.N40 (VCCGT), JCPU1.P33 (VCCGT), JCPU1.P34 (VCCGT), JCPU1.P36 (VCCGT), JCPU1.P38 (VCCGT), JCPU1.P40 (VCCGT), JCPU1.R34 (VCCGT), JCPU1.R35 (VCCGT), JCPU1.R36 (VCCGT), JCPU1.R37 (VCCGT), JCPU1.R38 (VCCGT), JCPU1.R39 (VCCGT), JCPU1.R40 (VCCGT), JCPU1.T33 (VCCGT), JCPU1.T34 (VCCGT), JCPU1.T36 (VCCGT), JCPU1.T38 (VCCGT), JCPU1.T40 (VCCGT), JCPU1.U34 (VCCGT), JCPU1.U35 (VCCGT), JCPU1.U36 (VCCGT), JCPU1.U37 (VCCGT), JCPU1.U38 (VCCGT), JCPU1.U39 (VCCGT), JCPU1.U40 (VCCGT), JCPU1.V33 (VCCGT), JCPU1.V34 (VCCGT), JCPU1.V36 (VCCGT), JCPU1.V38 (VCCGT), JCPU1.V40 (VCCGT), JCPU1.W34 (VCCGT), JCPU1.W35 (VCCGT), JCPU1.W36 (VCCGT), JCPU1.W37 (VCCGT), JCPU1.W38 (VCCGT), JCPU1.Y33 (VCCGT), JCPU1.Y34 (VCCGT), JCPU1.Y36 (VCCGT), JCPU1.Y38 (VCCGT); no longer JCPU1.AA34 (VCCGT), JCPU1.AA35 (VCCGT), JCPU1.AA36 (VCCGT), JCPU1.AA37 (VCCGT), JCPU1.AA38 (VCCGT), JCPU1.AB33 (VCCGT), JCPU1.AB34 (VCCGT), JCPU1.G36 (VCCGT), JCPU1.G37 (VCCGT), JCPU1.G38 (VCCGT), JCPU1.G39 (VCCGT), JCPU1.G40 (VCCGT), JCPU1.H36 (VCCGT), JCPU1.H38 (VCCGT), JCPU1.H40 (VCCGT), JCPU1.J36 (VCCGT), JCPU1.J37 (VCCGT), JCPU1.J38 (VCCGT), JCPU1.J39 (VCCGT), JCPU1.J40 (VCCGT), JCPU1.K36 (VCCGT), JCPU1.K38 (VCCGT), JCPU1.K40 (VCCGT), JCPU1.L34 (VCCGT), JCPU1.L35 (VCCGT), JCPU1.L36 (VCCGT), JCPU1.L37 (VCCGT), JCPU1.L38 (VCCGT), JCPU1.L39 (VCCGT), JCPU1.L40 (VCCGT), JCPU1.M33 (VCCGT), JCPU1.M34 (VCCGT), JCPU1.M36 (VCCGT), JCPU1.M38 (VCCGT), JCPU1.M40 (VCCGT), JCPU1.N34 (VCCGT), JCPU1.N35 (VCCGT), JCPU1.N36 (VCCGT), JCPU1.N37 (VCCGT), JCPU1.N38 (VCCGT), JCPU1.N39 (VCCGT), JCPU1.N40 (VCCGT), JCPU1.P33 (VCCGT), JCPU1.P34 (VCCGT), JCPU1.P36 (VCCGT), JCPU1.P38 (VCCGT), JCPU1.P40 (VCCGT), JCPU1.R34 (VCCGT), JCPU1.R35 (VCCGT), JCPU1.R36 (VCCGT), JCPU1.R37 (VCCGT), JCPU1.R38 (VCCGT), JCPU1.R39 (VCCGT), JCPU1.R40 (VCCGT), JCPU1.T33 (VCCGT), JCPU1.T34 (VCCGT), JCPU1.T36 (VCCGT), JCPU1.T38 (VCCGT), JCPU1.T40 (VCCGT), JCPU1.U34 (VCCGT), JCPU1.U35 (VCCGT), JCPU1.U36 (VCCGT), JCPU1.U37 (VCCGT), JCPU1.U38 (VCCGT), JCPU1.U39 (VCCGT), JCPU1.U40 (VCCGT), JCPU1.V33 (VCCGT), JCPU1.V34 (VCCGT), JCPU1.V36 (VCCGT), JCPU1.V38 (VCCGT), JCPU1.V40 (VCCGT), JCPU1.W34 (VCCGT), JCPU1.W35 (VCCGT), JCPU1.W36 (VCCGT), JCPU1.W37 (VCCGT), JCPU1.W38 (VCCGT), JCPU1.Y33 (VCCGT), JCPU1.Y34 (VCCGT), JCPU1.Y36 (VCCGT), JCPU1.Y38 (VCCGT)
- net VDDQ: now also JCPU1.AT18 (VDDQ), JCPU1.AT21 (VDDQ), JCPU1.AU13 (VDDQ), JCPU1.AU15 (VDDQ), JCPU1.AU19 (VDDQ), JCPU1.AU23 (VDDQ), JCPU1.AV11 (VDDQ), JCPU1.AV17 (VDDQ), JCPU1.AV21 (VDDQ), JCPU1.AW10 (VDDQ), JCPU1.AW14 (VDDQ), JCPU1.AW25 (VDDQ), JCPU1.AY12 (VDDQ), JCPU1.AY16 (VDDQ), JCPU1.AY18 (VDDQ), JCPU1.AY23 (VDDQ); no longer JCPU1.AT18 (VDDQ), JCPU1.AT21 (VDDQ), JCPU1.AU13 (VDDQ), JCPU1.AU15 (VDDQ), JCPU1.AU19 (VDDQ), JCPU1.AU23 (VDDQ), JCPU1.AV11 (VDDQ), JCPU1.AV17 (VDDQ), JCPU1.AV21 (VDDQ), JCPU1.AW10 (VDDQ), JCPU1.AW14 (VDDQ), JCPU1.AW25 (VDDQ), JCPU1.AY12 (VDDQ), JCPU1.AY16 (VDDQ), JCPU1.AY18 (VDDQ), JCPU1.AY23 (VDDQ)

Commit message: idek what i changed anymore but there's a bunch of new stuff lol
iirc i did some more misc cpu pins and a bunch of pch pcie stuff
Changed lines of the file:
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@@
 	(symbol
 		(lib_id "power:VCC")
-		(at 210.82 40.64 0)
+		(at 207.01 40.64 0)
 		(unit 1)
 		(exclude_from_sim no)
@@
 		(dnp no)
 		(property "Reference" "#PWR018"
-			(at 210.82 44.45 0)
+			(at 207.01 44.45 0)
 			(effects
 				(font
@@
 		)
 		(property "Value" "VCCST"
-			(at 210.82 36.83 0)
+			(at 207.01 36.83 0)
 			(effects
 				(font
@@
 		)
 		(property "Footprint" ""
-			(at 210.82 40.64 0)
+			(at 207.01 40.64 0)
 			(effects
 				(font
@@
 		)
 		(property "Datasheet" ""
-			(at 210.82 40.64 0)
+			(at 207.01 40.64 0)
 			(effects
 				(font
@@
 		)
 		(property "Description" "Power symbol creates a global label with name \"VCC\""
-			(at 210.82 40.64 0)
+			(at 207.01 40.64 0)
 			(effects
 				(font
@@
 	(symbol
 		(lib_id "power:VCC")
-		(at 203.2 40.64 0)
+		(at 214.63 40.64 0)
+		(unit 1)
+		(exclude_from_sim no)
+		(in_bom yes)
+		(on_board yes)
+		(dnp no)
+		(property "Reference" "#PWR046"
+			(at 214.63 44.45 0)
+			(effects
+				(font
+					(size 1.27 1.27)
+				)
+				(hide yes)
+			)
+		)
+		(property "Value" "VDDQ"
+			(at 214.63 36.83 0)
+			(effects
+				(font
+					(size 1.27 1.27)
+				)
+			)
+		)
+		(property "Footprint" ""
+			(at 214.63 40.64 0)
+			(effects
+				(font
+					(size 1.27 1.27)
+				)
+				(hide yes)
+			)
+		)
+		(property "Datasheet" ""
+			(at 214.63 40.64 0)
+			(effects
+				(font
+					(size 1.27 1.27)
+				)
+				(hide yes)
+			)
+		)
+		(property "Description" "Power symbol creates a global label with name \"VCC\""
+			(at 214.63 40.64 0)
+			(effects
+				(font
+					(size 1.27 1.27)
+				)
+				(hide yes)
+			)
+		)
+		(pin "1"
+		)
+		(instances
+			(project "Stroopwafel-LGA1151-CFL"
+				(path "/4bc771b8-eb19-46d0-8798-27231a7c6e83/5036d382-d60b-4069-a42a-4bbea2c68172"
+					(reference "#PWR046")
+					(unit 1)
+				)
+			)
+		)
+	)
+	(symbol
+		(lib_id "power:VCC")
+		(at 199.39 40.64 0)
 		(unit 1)
 		(exclude_from_sim no)
@@
 		(dnp no)
 		(property "Reference" "#PWR020"
-			(at 203.2 44.45 0)
+			(at 199.39 44.45 0)
 			(effects
 				(font
@@
 		)
 		(property "Value" "VCCIO"
-			(at 203.2 36.83 0)
+			(at 199.39 36.83 0)
 			(effects
 				(font
@@
 		)
 		(property "Footprint" ""
-			(at 203.2 40.64 0)
+			(at 199.39 40.64 0)
 			(effects
 				(font
@@
 		)
 		(property "Datasheet" ""
-			(at 203.2 40.64 0)
+			(at 199.39 40.64 0)
 			(effects
 				(font
@@
 		)
 		(property "Description" "Power symbol creates a global label with name \"VCC\""
-			(at 203.2 40.64 0)
+			(at 199.39 40.64 0)
 			(effects
 				(font
@@
 	(symbol
 		(lib_id "power:VCC")
-		(at 195.58 40.64 0)
+		(at 191.77 40.64 0)
 		(unit 1)
 		(exclude_from_sim no)
@@
 		(dnp no)
 		(property "Reference" "#PWR019"
-			(at 195.58 44.45 0)
+			(at 191.77 44.45 0)
 			(effects
 				(font
@@
 		)
 		(property "Value" "VCCSA"
-			(at 195.58 36.83 0)
+			(at 191.77 36.83 0)
 			(effects
 				(font
@@
 		)
 		(property "Footprint" ""
-			(at 195.58 40.64 0)
+			(at 191.77 40.64 0)
 			(effects
 				(font
@@
 		)
 		(property "Datasheet" ""
-			(at 195.58 40.64 0)
+			(at 191.77 40.64 0)
 			(effects
 				(font
@@
 		)
 		(property "Description" "Power symbol creates a global label with name \"VCC\""
-			(at 195.58 40.64 0)
+			(at 191.77 40.64 0)
 			(effects
 				(font
